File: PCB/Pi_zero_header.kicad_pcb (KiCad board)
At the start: 2 copper layers, 7 parts, among them J1 Raspberry_Pi_2_3, J2 USB_C_Receptacle_USB2.0, U1 RP2040, U2 W25Q128JVS, U3 TB6612FNG, U4 NCP1117-3.3_SOT223, U5 W25Q32JVSS

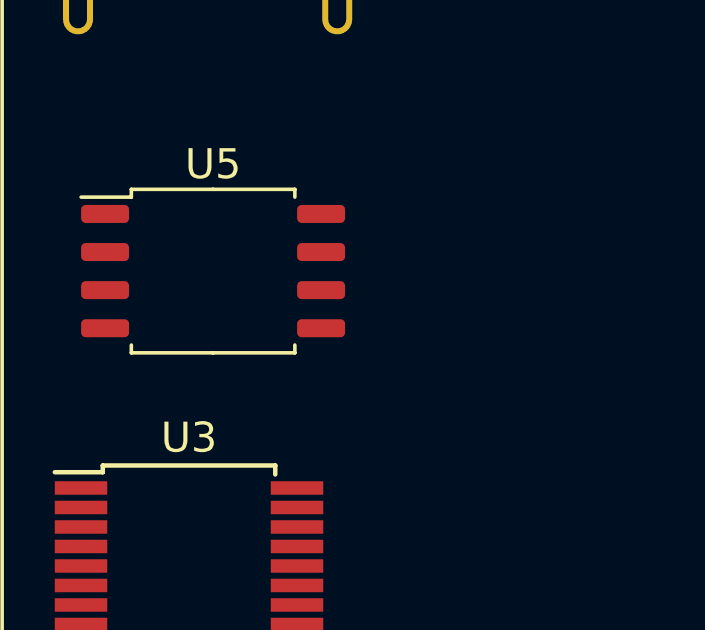
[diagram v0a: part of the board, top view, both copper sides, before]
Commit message: Updated and added TI charger
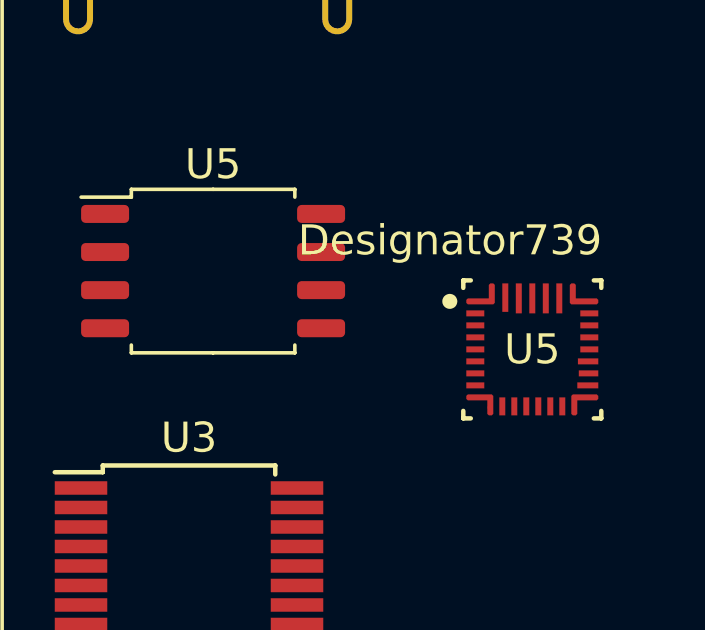
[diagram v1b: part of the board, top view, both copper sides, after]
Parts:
- added U5: BQ25672RQMR, RQM0029A-MFG:RQM0029A-MFG, F.Cu at (68.0, 76.9)

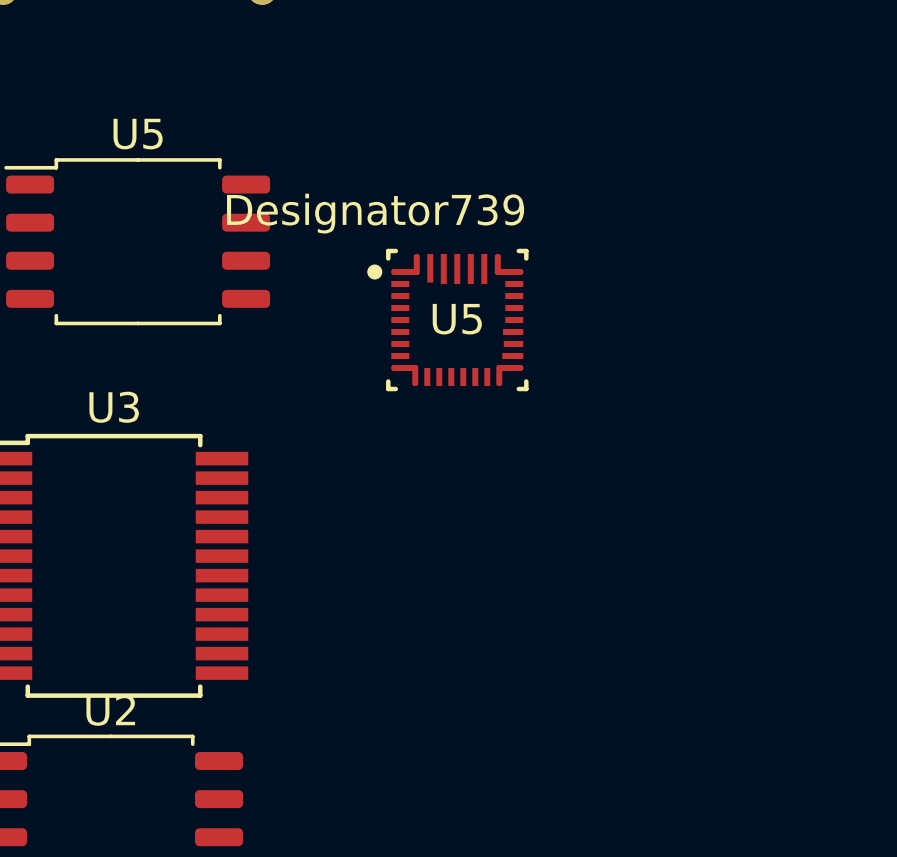
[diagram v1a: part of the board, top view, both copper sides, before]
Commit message: Moved added parts to corretc folders
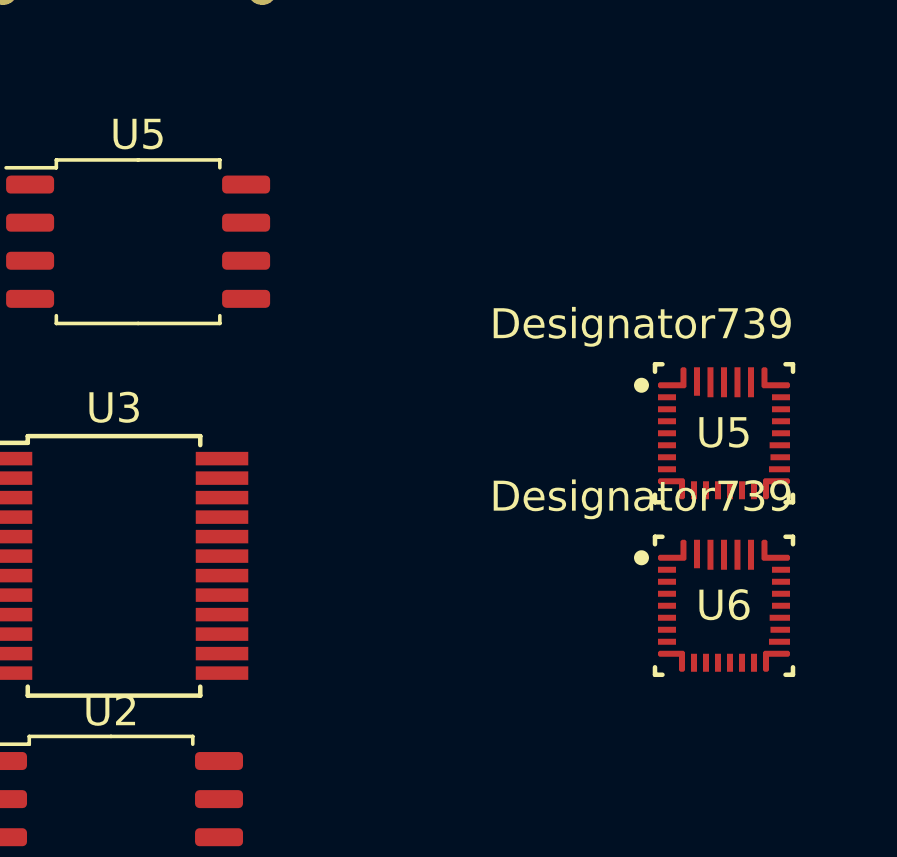
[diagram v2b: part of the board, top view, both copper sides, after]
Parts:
- added U6: PQ25792RQMR, RQM0029A-MFG:RQM0029A-MFG, F.Cu at (76.9, 86.4)
- moved U5 9.66 mm to (76.9, 80.7)

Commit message: Changed PCB design
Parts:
- removed the U5 at (57.4, 74.3)
- added H1: MountingHole, MountingHole:MountingHole_2.7mm_M2.5, F.Cu at (88.9, 37.6)
- added H2: MountingHole, MountingHole:MountingHole_2.7mm_M2.5, F.Cu at (88.9, 44.5)
- added H3: MountingHole, MountingHole:MountingHole_2.7mm_M2.5, F.Cu at (94.0, 81.3)
- added H4: MountingHole, MountingHole:MountingHole_2.7mm_M2.5, F.Cu at (68.6, 114.3)
- moved J2 49.9 mm to (58.4, 114.3)
- moved U3 22.3 mm to (65.0, 64.4)
- moved U5 19.0 mm to (58.4, 76.2)
- moved U4 14.7 mm to (56.2, 86.4)
- moved U6 14.3 mm to (66.2, 76.8)
- moved U2 11.4 mm to (67.5, 90.8)
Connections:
- J1 pad 1: +3V3 -> unconnected-(J1-3V3-Pad1)
- J1 pad 17: +3V3 -> unconnected-(J1-3V3-Pad17)
- J1 pad 2: VBUS -> +5V
- J1 pad 4: VBUS -> +5V
- U6 pad 10: unconnected-(U6-ACDRV2-Pad10) -> GND
- U6 pad 11: unconnected-(U6-ACDRV1-Pad11) -> GND
- U6 pad 14: unconnected-(U6-SCL-Pad14) -> /SCL_PWR
- U6 pad 15: unconnected-(U6-SDA-Pad15) -> /SDA_PWR
- U6 pad 2: unconnected-(U6-VBUS-Pad2) -> VBUS
- U6 pad 22: unconnected-(U6-BAT-Pad22) -> Net-(U6-BAT-Pad22)
- U6 pad 23: unconnected-(U6-BAT-Pad23) -> Net-(U6-BAT-Pad22)
- U6 pad 27: unconnected-(U6-GND-Pad27) -> GND
- U6 pad 29: unconnected-(U6-PMID-Pad29) -> Net-(U6-PMID)
- U6 pad 3: unconnected-(U6-VBUS-Pad3) -> VBUS
- U6 pad 6: unconnected-(U6-D+-Pad6) -> /USB_D+
- U6 pad 7: unconnected-(U6-D--Pad7) -> /USB_D-
- U6 pad 8: unconnected-(U6-VAC2-Pad8) -> Net-(U6-VAC1)
- U6 pad 9: unconnected-(U6-VAC1-Pad9) -> Net-(U6-VAC1)
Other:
- board outline added: 30 x 65 mm

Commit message: Update of PCB
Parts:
- removed U5: BQ25672RQMR, RQM0029A-MFG:RQM0029A-MFG
- moved H3 59.5 mm to (43.0, 112.0)
- moved H1 48.4 mm to (43.0, 53.0)
- moved H2 23.5 mm to (67.0, 53.0)
- moved H4 2.79 mm to (67.0, 112.0)

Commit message: Some changes
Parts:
- removed U4: NCP1117-3.3_SOT223, Package_TO_SOT_SMD:SOT-223-3_TabPin2
- added J3: Screw_Terminal_01x02, TerminalBlock_TE-Connectivity:TerminalBlock_TE_282834-2_1x02_P2.54mm_Horizontal, F.Cu at (66.5, 88.9)
- added J4: Screw_Terminal_01x02, TerminalBlock_TE-Connectivity:TerminalBlock_TE_282834-2_1x02_P2.54mm_Horizontal, F.Cu at (66.5, 81.3)
- added SW1: SW_Push, Button_Switch_SMD:SW_Push_1P1T_NO_Vertical_Wuerth_434133025816, F.Cu at (56.5, 66.5)
- moved U3 35.1 mm to (63.5, 99.5), turned to -90 degrees
- moved U6 29.5 mm to (51.9, 102.6), turned to 90 degrees
- moved U1 21.3 mm to (56.4, 82.4)
- moved U2 20.2 mm to (56.4, 73.9)
- moved J1 5.50 mm to (44.8, 58.4)
- moved J2 4.42 mm to (55.0, 111.5)
- moved H1 0.71 mm to (43.5, 53.5)
- moved H2 0.71 mm to (66.5, 53.5)
- moved H3 0.71 mm to (43.5, 111.5)
- moved H4 0.71 mm to (66.5, 111.5)
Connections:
- U3 pad 13: +5V -> VDD
- U3 pad 14: +5V -> VDD
- U3 pad 24: +5V -> VDD
- U6 pad 1: unconnected-(U6-STAT-Pad1) -> Net-(D1-K)
- U6 pad 18: unconnected-(U6-BATP-Pad18) -> Net-(U6-BATP)
- U6 pad 19: unconnected-(U6-BTST2-Pad19) -> Net-(U6-BTST2)
- U6 pad 21: unconnected-(U6-INT_N-Pad21) -> /INT_N
- U6 pad 24: unconnected-(U6-SDRV-Pad24) -> Net-(U6-SDRV)
- U6 pad 25: unconnected-(U6-SYS-Pad25) -> VDD
- U6 pad 26: unconnected-(U6-SW2-Pad26) -> Net-(U6-SW2)
- U6 pad 28: unconnected-(U6-SW1-Pad28) -> Net-(U6-SW1)
- U6 pad 4: unconnected-(U6-BTST1-Pad4) -> Net-(U6-BTST1)
- U6 pad 5: unconnected-(U6-REGN-Pad5) -> /REGN

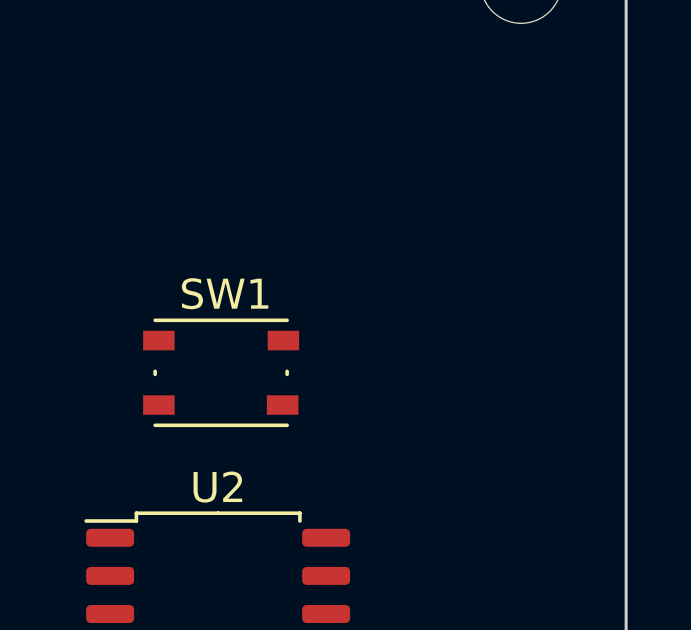
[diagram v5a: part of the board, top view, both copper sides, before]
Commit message: Added buck-boost converter to schema
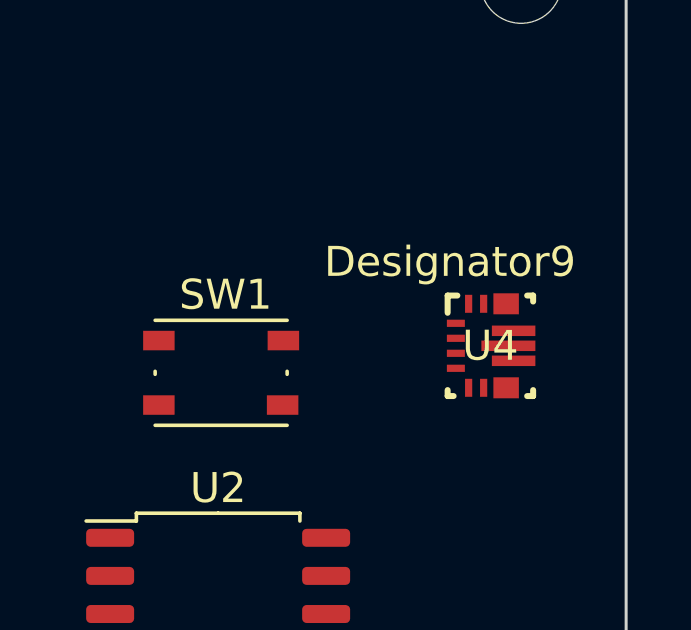
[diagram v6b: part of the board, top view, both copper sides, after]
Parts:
- added U4: TPS630701RNMR, RNM0015A:RNM0015A, F.Cu at (65.5, 65.6)
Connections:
- U6 pad 16: unconnected-(U6-TS-Pad16) -> Net-(U6-TS)
- U6 pad 17: unconnected-(U6-ILIM_HIZ-Pad17) -> Net-(U6-ILIM_HIZ)
- U6 pad 20: unconnected-(U6-PROG-Pad20) -> Net-(U6-PROG)
- U6 pad 6: /USB_D+ -> unconnected-(U6-D+-Pad6)
- U6 pad 7: /USB_D- -> unconnected-(U6-D--Pad7)

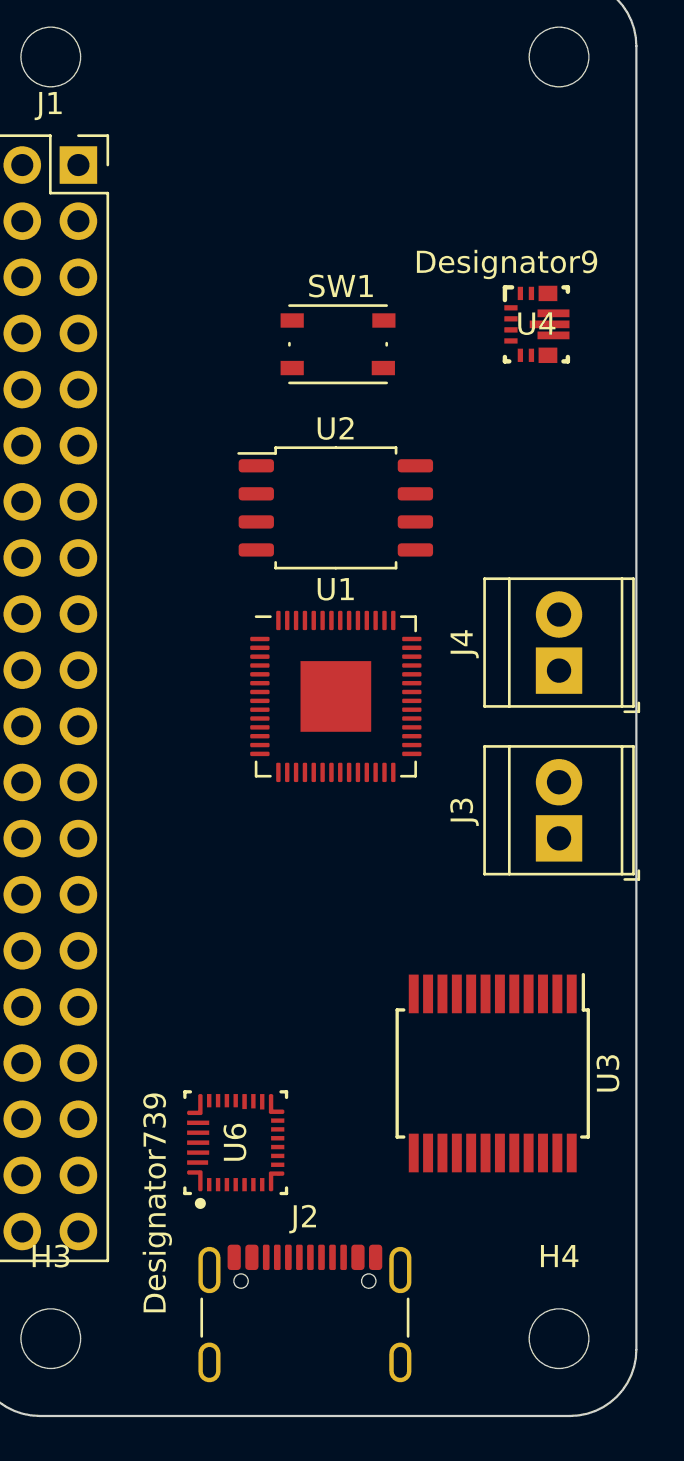
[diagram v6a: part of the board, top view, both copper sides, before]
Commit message: Added second buck-boost converter
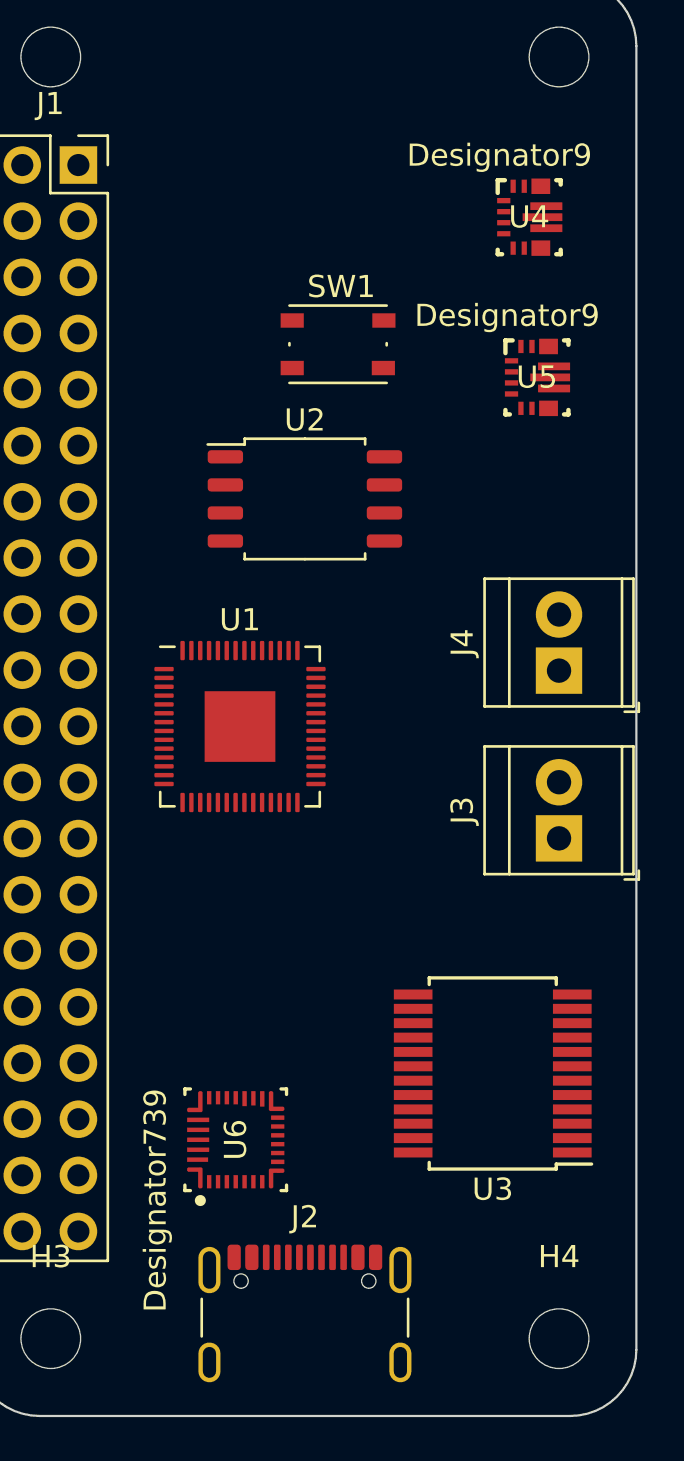
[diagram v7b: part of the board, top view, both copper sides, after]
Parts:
- added U5: TPS630701RNMR, RNM0015A:RNM0015A, F.Cu at (65.5, 68.0)
- moved U4 4.86 mm to (65.2, 60.8)
- moved U1 4.55 mm to (52.1, 83.8)
- moved U2 1.46 mm to (55.0, 73.5)
- moved U6 0.13 mm to (51.9, 102.5)
- turned U3 to 180 degrees
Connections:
- U4 pad 1: unconnected-(U4-PS_SYNC-Pad1) -> Net-(U4-EN)
- U4 pad 10: unconnected-(U4-PGND-Pad10) -> GND
- U4 pad 11: unconnected-(U4-L1-Pad11) -> Net-(U4-L1)
- U4 pad 12: unconnected-(U4-VIN-Pad12) -> VDD
- U4 pad 13: unconnected-(U4-VIN-Pad13) -> VDD
- U4 pad 14: unconnected-(U4-EN-Pad14) -> Net-(U4-EN)
- U4 pad 15: unconnected-(U4-VSEL-Pad15) -> GND
- U4 pad 2: unconnected-(U4-PG-Pad2) -> Net-(U4-PG)
- U4 pad 3: unconnected-(U4-VAUX-Pad3) -> Net-(U4-VAUX)
- U4 pad 4: unconnected-(U4-GND-Pad4) -> GND
- U4 pad 5: unconnected-(U4-FB-Pad5) -> Net-(U4-FB)
- U4 pad 6: unconnected-(U4-FB2-Pad6) -> GND
- U4 pad 7: unconnected-(U4-VOUT-Pad7) -> +5V
- U4 pad 8: unconnected-(U4-VOUT-Pad8) -> +5V
- U4 pad 9: unconnected-(U4-L2-Pad9) -> Net-(U4-L2)

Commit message: Hopefully done schema
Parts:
- added J5: Conn_02x04_Top_Bottom, Connector_PinHeader_2.54mm:PinHeader_2x04_P2.54mm_Horizontal, F.Cu at (63.5, 58.5)
- added J7: Conn_01x04, Connector_PinHeader_2.54mm:PinHeader_1x04_P2.54mm_Horizontal, F.Cu at (89.6, 55.2)
- added J8: Conn_02x03_Top_Bottom, Connector_PinHeader_2.54mm:PinHeader_2x03_P2.54mm_Horizontal, F.Cu at (82.3, 80.0)
- added J9: Conn_01x02, Connector_PinHeader_2.54mm:PinHeader_1x02_P2.54mm_Horizontal, F.Cu at (82.6, 95.7)
- added SW2: SW_Push, Button_Switch_SMD:SW_Push_1P1T_NO_Vertical_Wuerth_434133025816, F.Cu at (50.5, 59.4)
- added SW3: SW_SPST, Button_Switch_THT:SW_DIP_SPSTx01_Piano_10.8x4.1mm_W7.62mm_P2.54mm, F.Cu at (68.5, 104.0)
- moved U5 13.0 mm to (52.6, 65.8)
- moved U3 10.4 mm to (55.0, 93.5)
- moved U4 8.90 mm to (58.1, 66.3)
- moved SW1 7.42 mm to (56.5, 59.1)
- moved U1 2.84 mm to (54.2, 81.9)
- moved U6 1.50 mm to (50.4, 102.5)
- moved U2 1.12 mm to (54.0, 73.0)
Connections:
- net Net-(C29-Pad1) renamed +BATT
- J1 pad 19: unconnected-(J1-MOSI0/GPIO10-Pad19) -> /MOSI_RPi
- J1 pad 21: unconnected-(J1-MISO0/GPIO9-Pad21) -> /MISO_RPi
- J1 pad 23: unconnected-(J1-SCLK0/GPIO11-Pad23) -> /SCLK_RPi
- J1 pad 24: unconnected-(J1-~{CE0}/GPIO8-Pad24) -> /CE_N_RPI
- J1 pad 32: unconnected-(J1-PWM0/GPIO12-Pad32) -> Net-(J1-PWM0/GPIO12)
- J1 pad 33: unconnected-(J1-PWM1/GPIO13-Pad33) -> Net-(J1-PWM1/GPIO13)
- U1 pad 11: unconnected-(U1-GPIO8-Pad11) -> /MOSI_RPi
- U1 pad 12: unconnected-(U1-GPIO9-Pad12) -> /SCLK_RPi
- U1 pad 2: unconnected-(U1-GPIO0-Pad2) -> Net-(J5-Pin_3)
- U1 pad 26: unconnected-(U1-RUN-Pad26) -> Net-(U1-RUN)
- U1 pad 28: unconnected-(U1-GPIO17-Pad28) -> Net-(J8-Pin_4)
- U1 pad 29: unconnected-(U1-GPIO18-Pad29) -> Net-(J8-Pin_1)
- U1 pad 3: unconnected-(U1-GPIO1-Pad3) -> Net-(J5-Pin_4)
- U1 pad 30: unconnected-(U1-GPIO19-Pad30) -> /PWMA
- U1 pad 31: unconnected-(U1-GPIO20-Pad31) -> /PWMB
- U1 pad 32: unconnected-(U1-GPIO21-Pad32) -> /AIN1
- U1 pad 34: unconnected-(U1-GPIO22-Pad34) -> /AIN2
- U1 pad 35: unconnected-(U1-GPIO23-Pad35) -> /BIN1
- U1 pad 36: unconnected-(U1-GPIO24-Pad36) -> /BIN2
- U1 pad 37: unconnected-(U1-GPIO25-Pad37) -> /STBY_N
- U1 pad 4: unconnected-(U1-GPIO2-Pad4) -> /SCL_PWR
- U1 pad 5: unconnected-(U1-GPIO3-Pad5) -> /SDA_PWR
- U1 pad 56: unconnected-(U1-QSPI_SS-Pad56) -> /QSPI_SS
- U1 pad 6: unconnected-(U1-GPIO4-Pad6) -> /CE_N_PWR
- U1 pad 7: unconnected-(U1-GPIO5-Pad7) -> /QON_N_PWR
- U1 pad 8: unconnected-(U1-GPIO6-Pad8) -> /CE_N_RPI
- U1 pad 9: unconnected-(U1-GPIO7-Pad9) -> /MISO_RPi
- U2 pad 1: Net-(U2-~{CS}) -> /QSPI_SS
- U3 pad 15: unconnected-(U3-PWMB-Pad15) -> /PWMB
- U3 pad 16: unconnected-(U3-BIN2-Pad16) -> /BIN2
- U3 pad 17: unconnected-(U3-BIN1-Pad17) -> /BIN1
- U3 pad 19: unconnected-(U3-STBY-Pad19) -> /STBY_N
- U3 pad 21: unconnected-(U3-AIN1-Pad21) -> /AIN1
- U3 pad 22: unconnected-(U3-AIN2-Pad22) -> /AIN2
- U3 pad 23: unconnected-(U3-PWMA-Pad23) -> /PWMA
- U6 pad 12: unconnected-(U6-QON_N-Pad12) -> /QON_N_PWR
- U6 pad 13: unconnected-(U6-CE_N-Pad13) -> /CE_N_PWR
- U6 pad 25: VDD -> Net-(SW3-A)
